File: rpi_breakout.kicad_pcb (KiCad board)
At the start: 2 copper layers, 65 x 30 mm, 31 parts, among them J1 R22, J11 R22, J14 Raspberry_Pi_2_3, J17 Raspberry_Pi_2_3, J18 R22, J19 R22, J3 R22, J5 R22, J7 R22, J9 R22

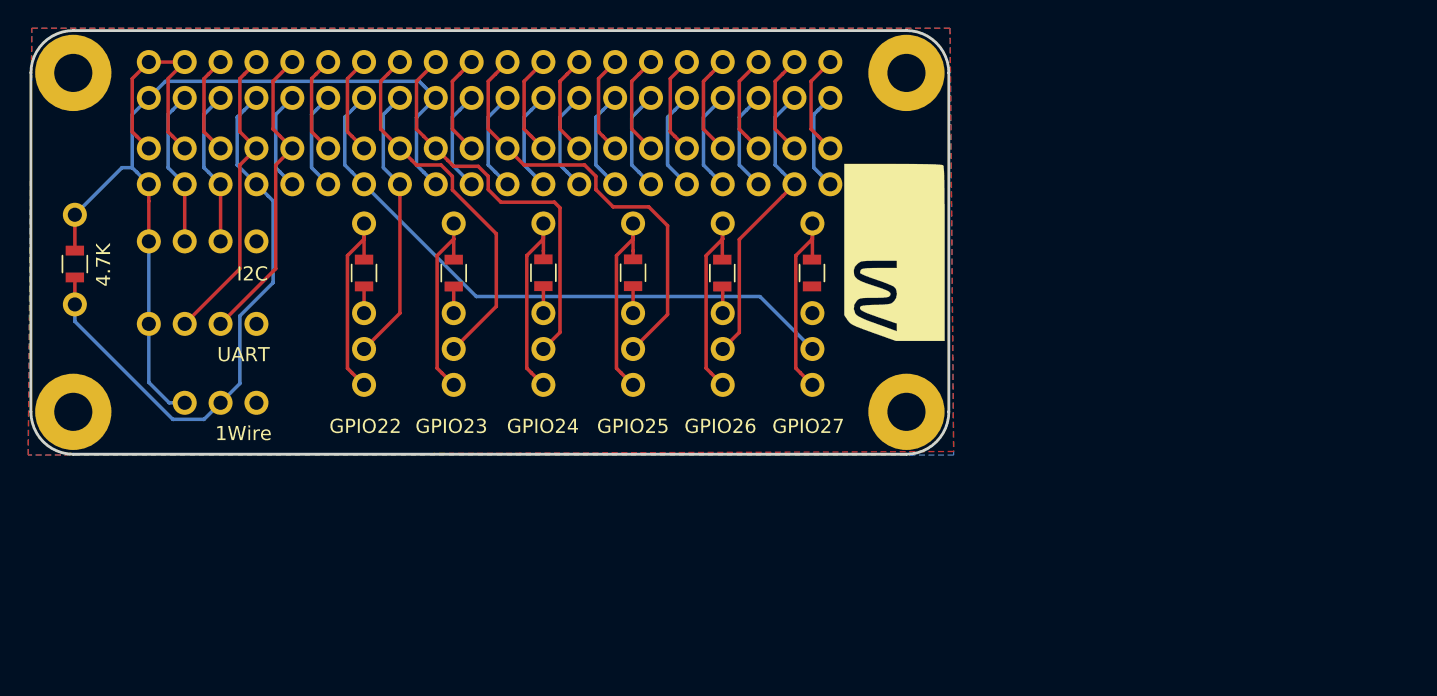
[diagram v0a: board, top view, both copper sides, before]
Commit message: Fix corner mounting holes, increase spacing b/w headers. Tag 1.1
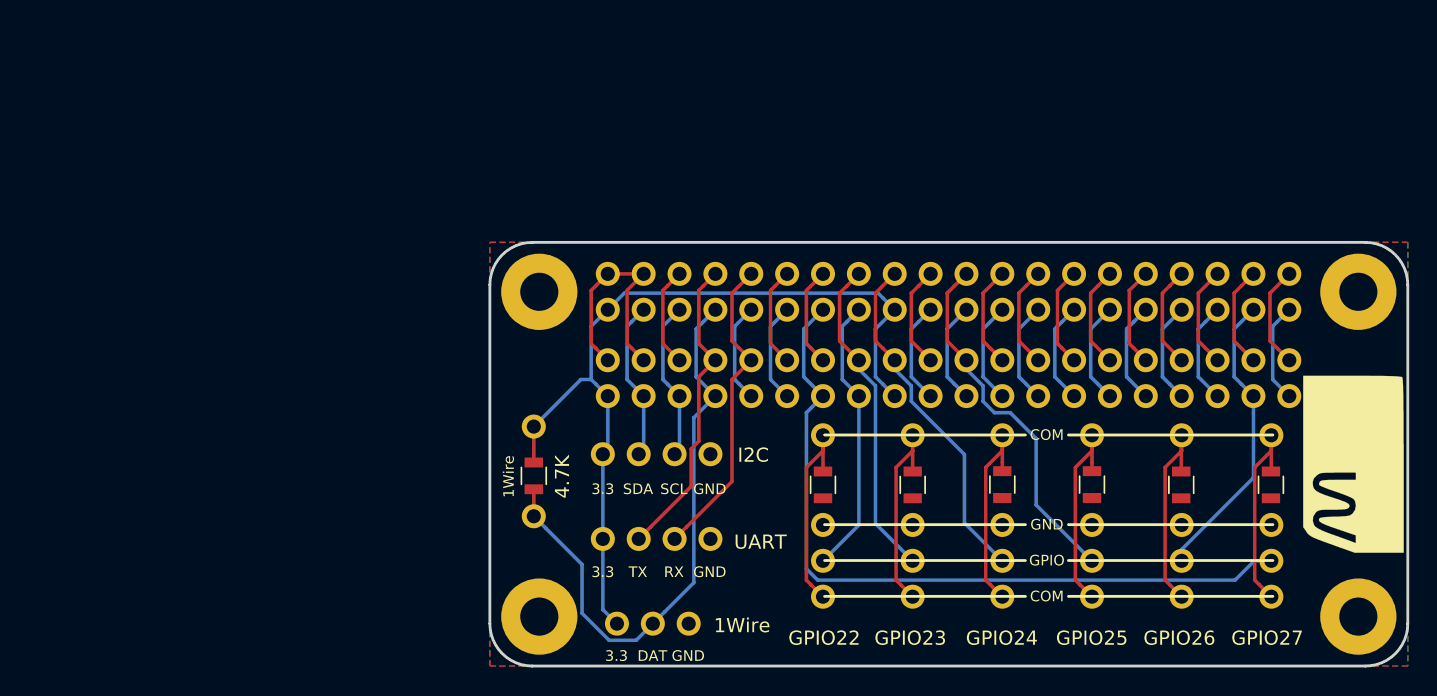
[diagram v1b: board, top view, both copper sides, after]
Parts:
- REF**: moved to B.Cu
- moved REF** 36.5 mm to (103.5, 103.5)
- moved REF** 36.0 mm to (103.5, 126.5)
- moved GPIO26 35.8 mm to (149.0, 120.0)
- moved J5 35.8 mm to (149.0, 113.7)
- moved 4.7K 35.8 mm to (103.1, 116.5)
- moved G*** 35.8 mm to (161.2, 115.7)
- moved GPIO22 35.8 mm to (123.6, 120.0)
- moved GPIO23 35.8 mm to (129.9, 120.0)
- moved GPIO27 35.8 mm to (155.3, 120.0)
- moved J1 35.8 mm to (123.6, 113.7)
- moved J11 35.8 mm to (155.3, 113.7)
- moved J14 35.8 mm to (108.3, 104.8)
- moved J17 35.8 mm to (108.3, 110.9)
- moved J18 35.8 mm to (103.1, 119.4)
- moved J19 35.8 mm to (103.1, 113.0)
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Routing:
- net 13: track 43.8 -> 53.8 mm
- net GND: track 66.8 -> 57.4 mm
- net 22: track 31.1 -> 25.8 mm
- net 18: track 28.8 -> 24.6 mm
- net 16: track 26.5 -> 23.0 mm
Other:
- board text added: "1Wire"
- board text added: "3.3"
- board text added: "COM"
- board text added: "DAT"
- board text added: "GND"
- board text added: "GPIO"
- board text added: "RX"
- board text added: "SCL"
- board text added: "SDA"
- board text added: "TX"
- board text added: "v1.1"
- board text removed: "v1.0"
